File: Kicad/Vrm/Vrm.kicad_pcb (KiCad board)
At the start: 2 copper layers, 94 x 100.3 mm, 44 parts, among them U1 STM32F091RCTx

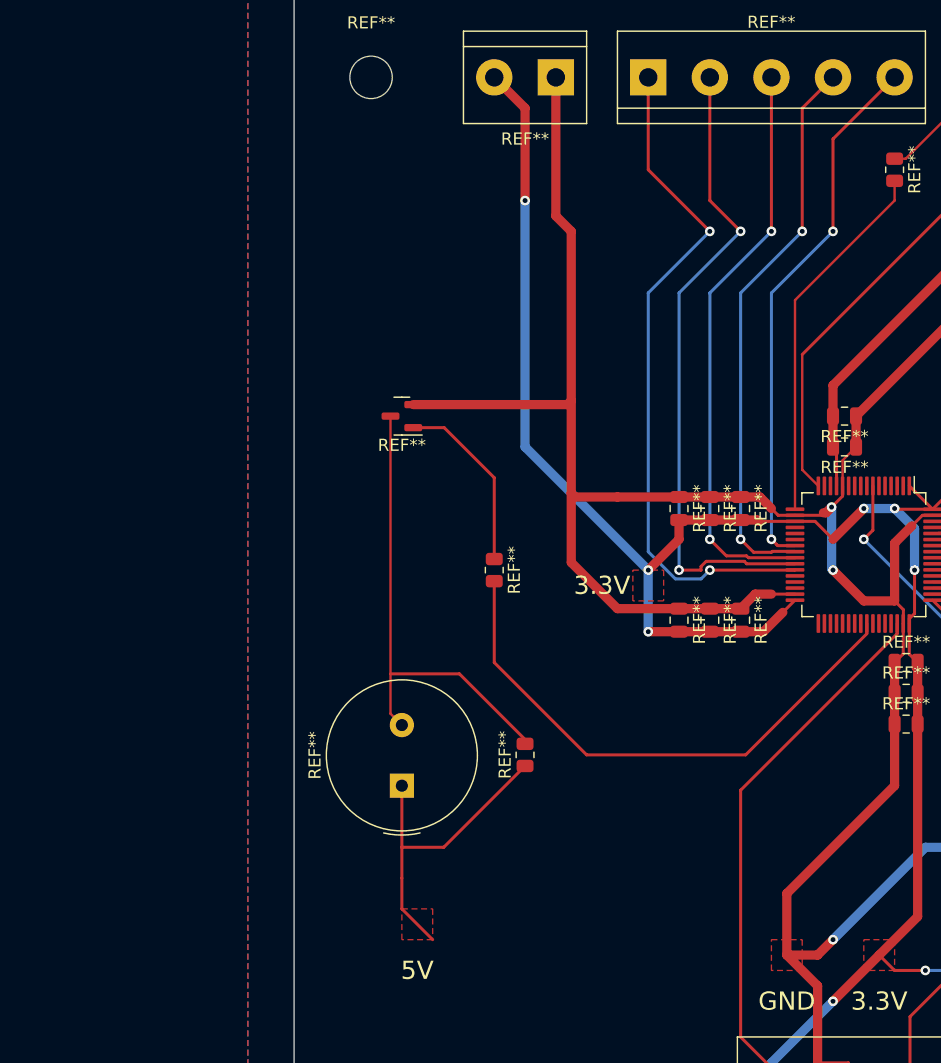
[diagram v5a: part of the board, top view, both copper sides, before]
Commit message: Added power modules to PCB
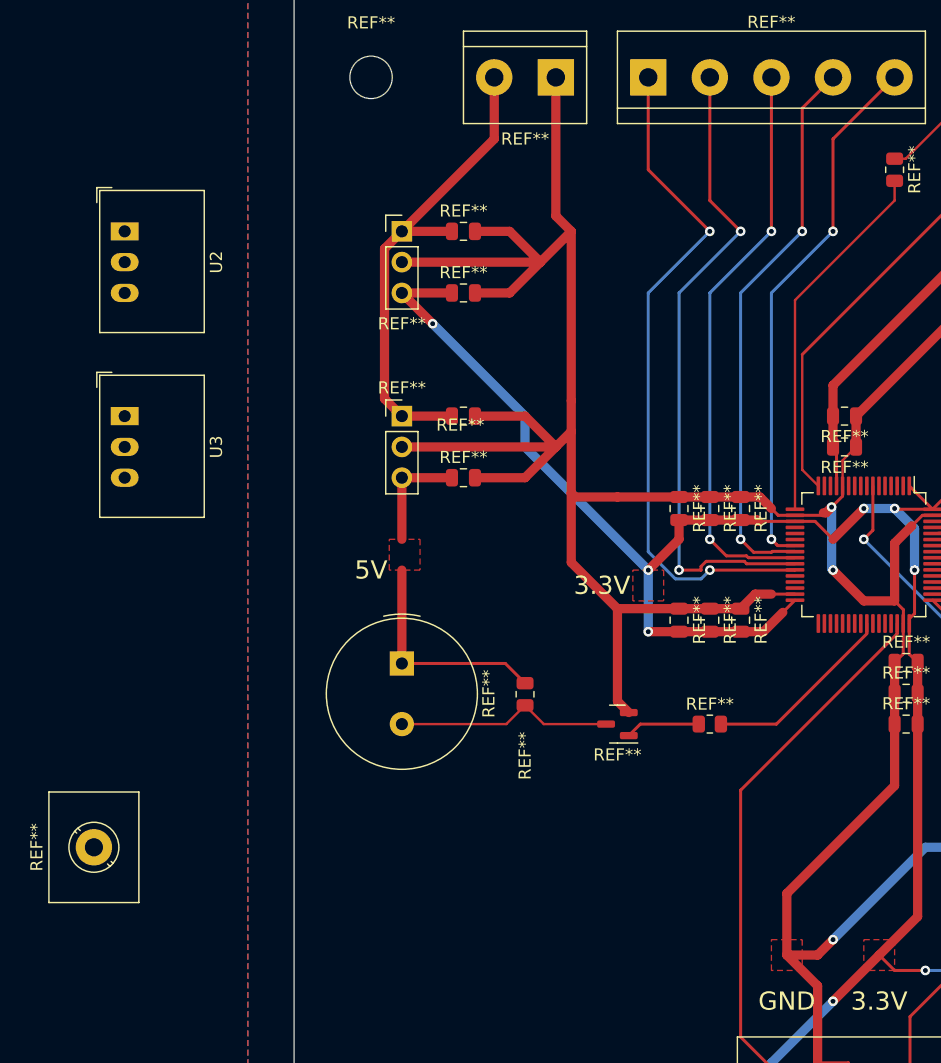
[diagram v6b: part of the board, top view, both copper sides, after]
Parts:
- added REF**: Servo UART (Extra), TerminalBlock_MetzConnect:TerminalBlock_MetzConnect_360271_1x01_Horizontal_ScrewM3.0_Boxed, F.Cu at (111.8, 124.5)
- added REF**: 10nF, Capacitor_SMD:C_0805_2012Metric, F.Cu at (142.2, 73.7)
- added REF**: 10nF, Capacitor_SMD:C_0805_2012Metric, F.Cu at (142.2, 88.9)
- added REF**: 10nF, Capacitor_SMD:C_0805_2012Metric, F.Cu at (142.2, 78.7)
- added REF**: 5V Header, Connector_PinHeader_2.54mm:PinHeader_1x03_P2.54mm_Vertical, F.Cu at (137.2, 88.9)
- added REF**: 10nF, Capacitor_SMD:C_0805_2012Metric, F.Cu at (142.2, 94.0)
- added REF**: VDD Header, Connector_PinHeader_2.54mm:PinHeader_1x03_P2.54mm_Vertical, F.Cu at (137.2, 73.7)
- added U2: R-78E3.3-0.5, Converter_DCDC:Converter_DCDC_RECOM_R-78E-0.5_THT, F.Cu at (114.3, 73.7)
- added U3: R-78E5.0-0.5, Converter_DCDC:Converter_DCDC_RECOM_R-78E-0.5_THT, F.Cu at (114.3, 88.9)
- REF**: value VDD GND -> 7.5V GND
- moved REF** 31.0 mm to (154.9, 114.3)
- moved REF** 21.8 mm to (162.6, 114.3), turned to 0 degrees
- moved REF** 10.1 mm to (137.2, 109.3), turned to -90 degrees
- moved REF** 5.00 mm to (147.3, 111.8), turned to -90 degrees
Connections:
- REF** pad 1: (no net) -> 5V (x2)
- REF** pad 2: VDD -> +7.5V
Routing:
- net GND: track 352.6 -> 406.3 mm
- net (no net): track 212.9 -> 164.8 mm
- net +7.5V: track 0.00 -> 40.5 mm
- net Buzzer Module: track 45.6 -> 16.0 mm
- net 5V: track 0.00 -> 27.7 mm
- net VDD: track 190.6 -> 180.1 mm
- net unconnected-(Q1-Pad2): track 15.1 -> 6.16 mm
- added copper zone on F.Cu, net 5V
- removed copper zone on F.Cu, net (none)

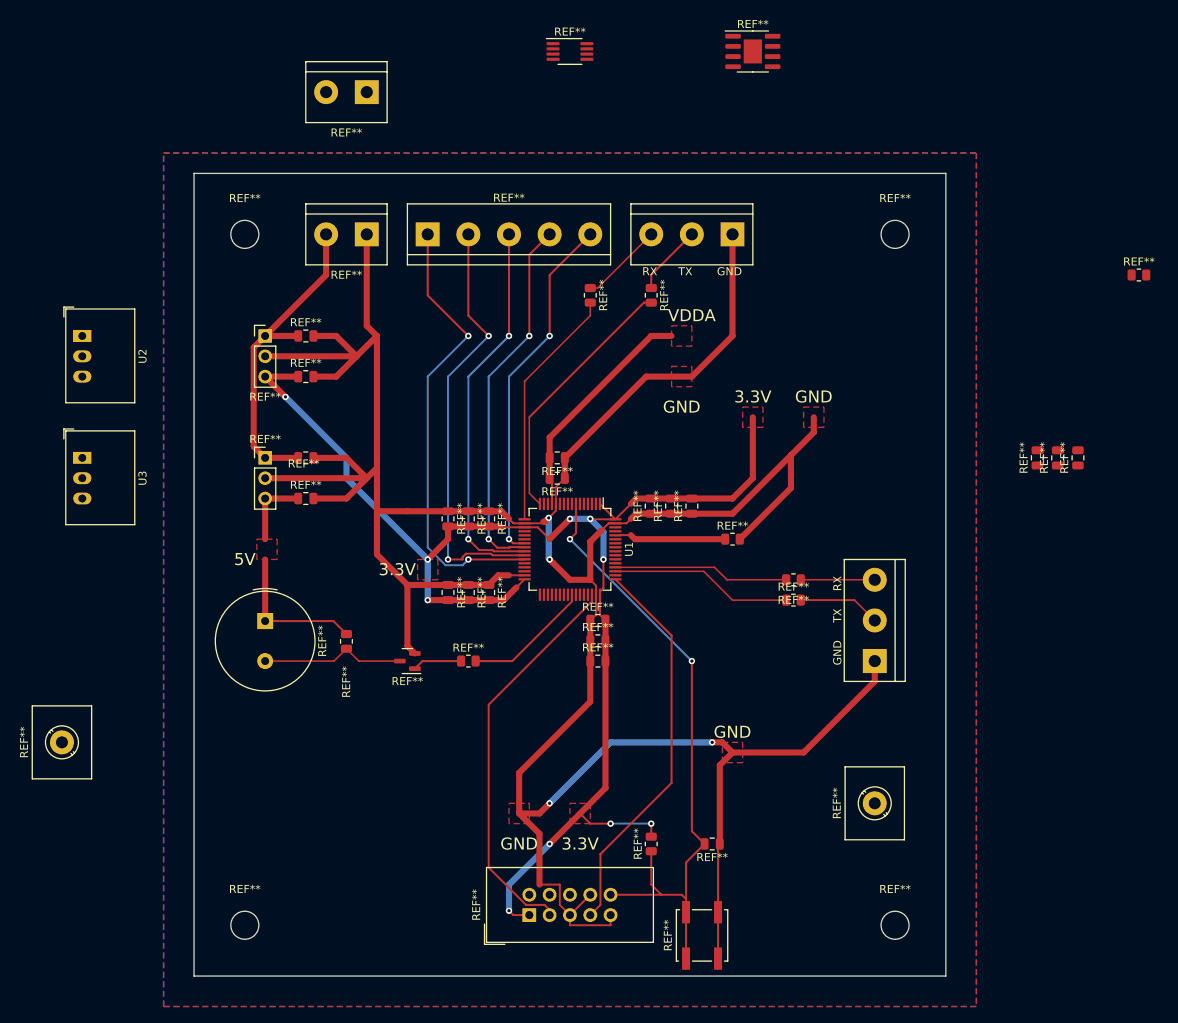
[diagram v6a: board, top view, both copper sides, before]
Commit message: Added VDD connections
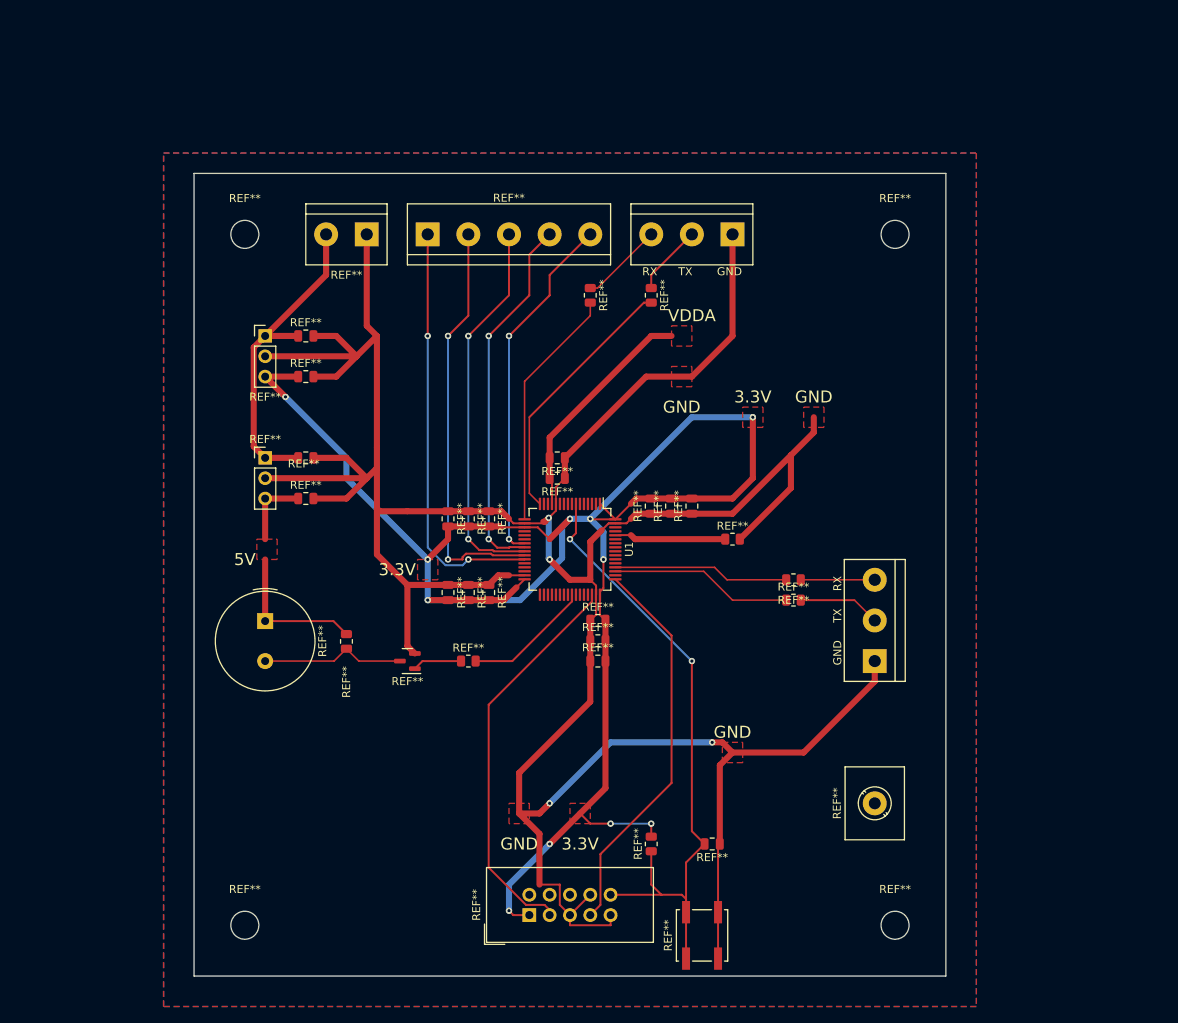
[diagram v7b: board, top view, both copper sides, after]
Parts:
- removed the REF** at (149.9, 43.2)
- removed the REF** at (198.1, 38.1)
- removed the REF** at (111.8, 124.5)
- removed the REF** at (246.4, 66.0)
- removed the REF** at (175.3, 38.1)
- removed the REF** at (238.8, 88.9)
- removed the REF** at (236.2, 88.9)
- removed the REF** at (233.7, 88.9)
- removed U2: R-78E3.3-0.5, Converter_DCDC:Converter_DCDC_RECOM_R-78E-0.5_THT
- removed U3: R-78E5.0-0.5, Converter_DCDC:Converter_DCDC_RECOM_R-78E-0.5_THT
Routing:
- net VDD: track 180.1 -> 230.0 mm, vias 10 -> 11
- net unconnected-(U1-Pad27): track 56.7 -> 52.5 mm
- net unconnected-(U1-Pad26): track 53.9 -> 51.8 mm

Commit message: Added pads
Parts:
- added REF**: VDDA Pad, TestPoint:TestPoint_Pad_3.0x3.0mm, F.Cu at (188.0, 73.7)
- added REF**: 3.3V Pad, TestPoint:TestPoint_Pad_3.0x3.0mm, F.Cu at (177.8, 132.1)
- added REF**: GND Pad, TestPoint:TestPoint_Pad_3.0x3.0mm, F.Cu at (188.0, 78.7)
- added REF**: 3.3V Pad, TestPoint:TestPoint_Pad_3.0x3.0mm, F.Cu at (198.1, 83.8)
- added REF**: GND Pad, TestPoint:TestPoint_Pad_3.0x3.0mm, F.Cu at (205.7, 83.8)
- added REF**: 5V Pad, TestPoint:TestPoint_Pad_3.0x3.0mm, F.Cu at (137.2, 101.6)
- added REF**: GND Pad, TestPoint:TestPoint_Pad_3.0x3.0mm, F.Cu at (195.6, 124.5)
- added REF**: GND Pad, TestPoint:TestPoint_Pad_3.0x3.0mm, F.Cu at (170.2, 132.1)
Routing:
- net 5V: track 27.7 -> 30.3 mm
- removed copper zone on F.Cu, net 5V
- removed copper zone on F.Cu, net VDD
- removed copper zone on F.Cu, net VDDA
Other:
- board text added: "1"
- board text removed: "5V"
- board text removed: "GND"
- board text removed: "VDDA"
